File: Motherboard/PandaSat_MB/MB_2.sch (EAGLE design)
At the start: 70 parts, among them J1 503182-1852, J2 10118194-0001LF, J3 DCJ0303, Q10 IRLML5103, Q11 IRLML5103, Q13 IRLML2803, Q14 IRLML2803, Q15 IRLML2803, Q16 IRLML5103, Q17 2N5088, U1 MAX706R, U20 MR25H40MDF, U3 LSM9DS1, U4 PE014006, U5 MAX4372TEUK+T, U6 RFM23BP, U7 TPS54226PWPRPWP14_2P31X2P46-L, U8 ATSAMD51, X1 BU-SMA-V

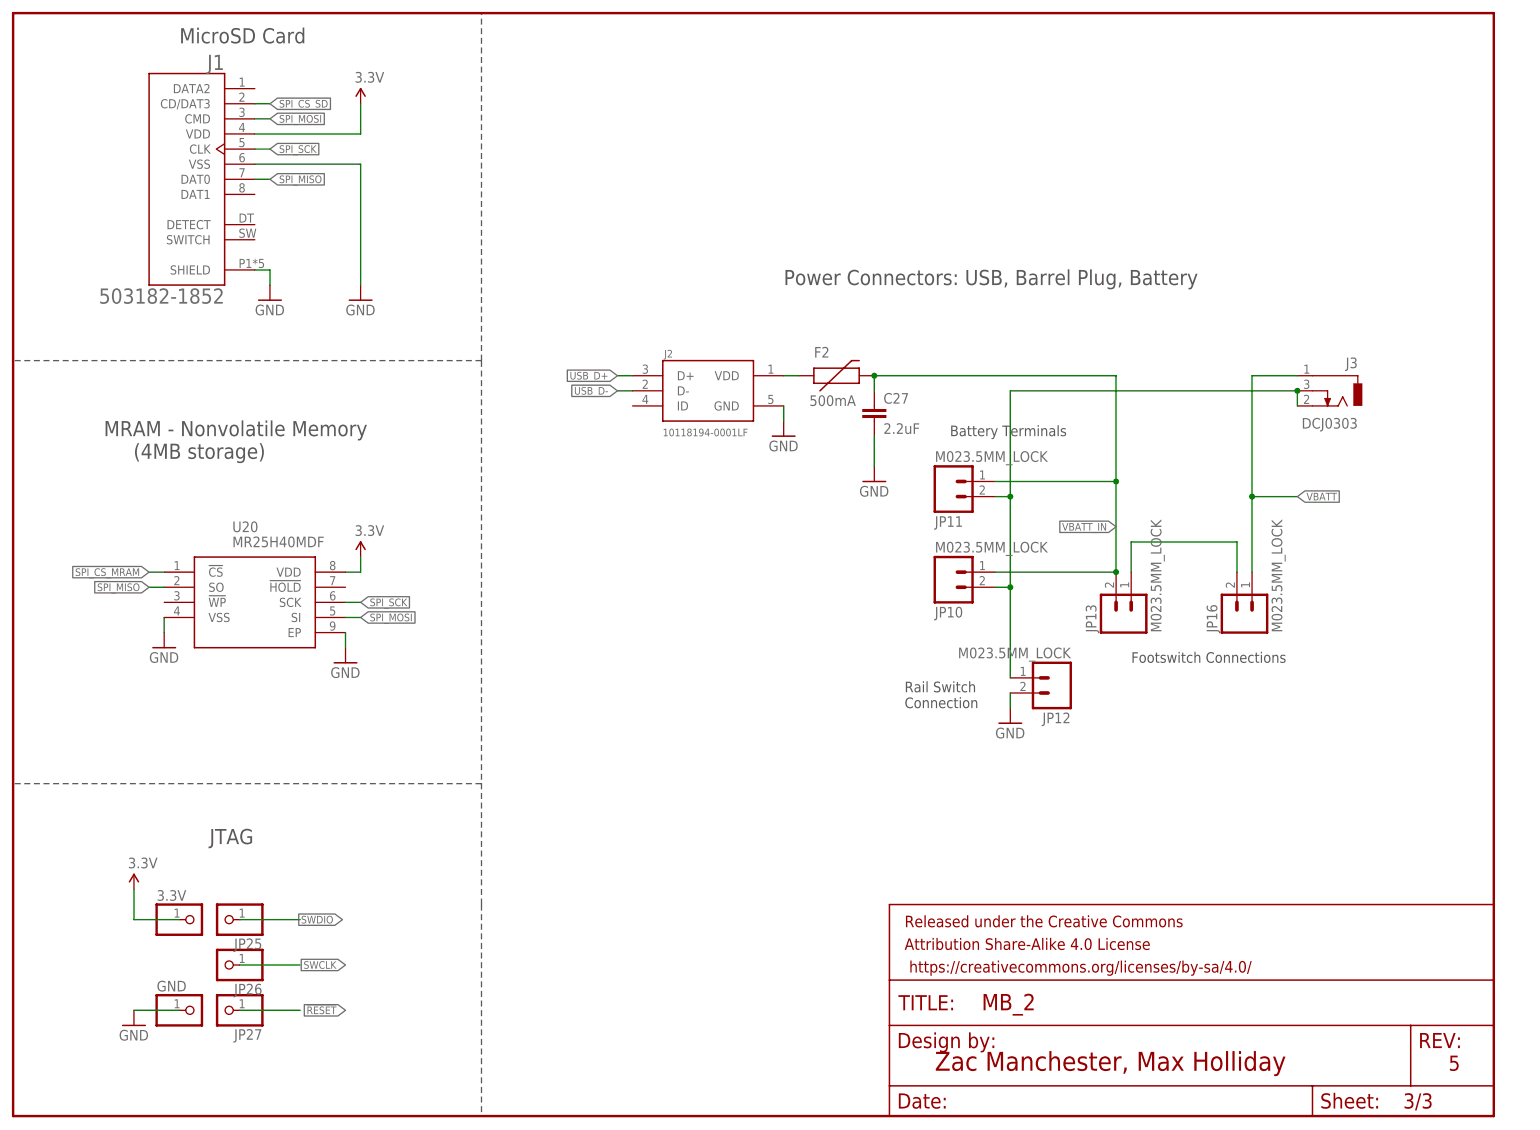
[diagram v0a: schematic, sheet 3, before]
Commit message: Added datasheets
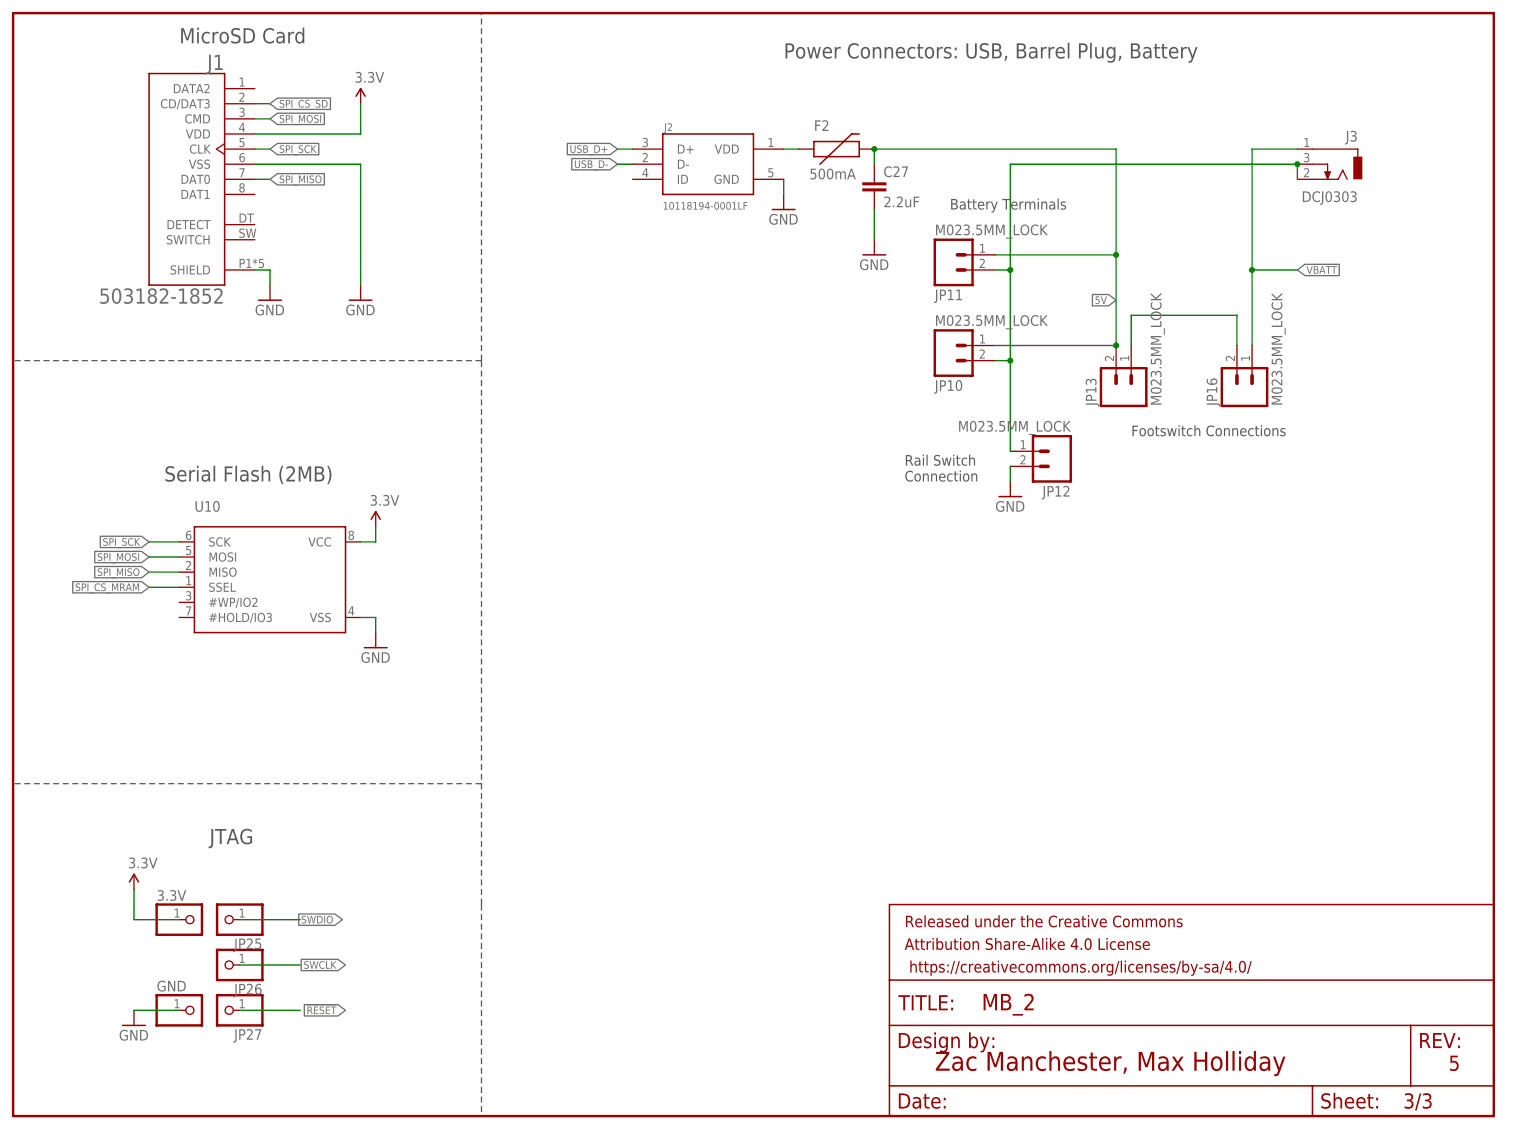
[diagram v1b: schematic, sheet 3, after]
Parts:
- removed U20: MR25H40MDF, maholli:MR25H40MDF
- added JP5: JUMPER-PAD-3-2OF3_NC_BY_TRACE_SMALL, SparkFun-Passives:JUMPER-PAD-3-2OF3_NC_BY_TRACE_SMALL
- added U10: (no value), microbuilder:SPIFLASH_SOIC8
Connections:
- removed net VBATT_IN: C27.1, F2.2, JP10.1, JP11.1, JP13.2
- new net 5V: C27.1, F2.2, JP10.1, JP11.1, JP13.2, U6.VCC
- new net N$1: JP5.2, U1.!WDO
- new net N$5: JP5.1, U1.!RESET
- net !RESET: now also JP5.3; no longer U1.!RESET, U1.!WDO
- net 3.3V: now also U10.VCC; no longer U20.VDD, U6.VCC
- net GND: now also U10.VSS; no longer U20.EP, U20.VSS
- net SPI_CS_MRAM: now also U10.SSEL; no longer U20.!CS
- net SPI_MISO: now also U10.MISO; no longer U20.SO
- net SPI_MOSI: now also U10.MOSI; no longer U20.SI
- net SPI_SCK: now also U10.SCK; no longer U20.SCK
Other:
- note added: "Serial Flash (2MB)"
- note removed: "MRAM - Nonvolatile Memory (4MB storage)"
- moved on the sheet: C27, F2, J2, J3, JP10, JP11, JP12, JP13, JP16

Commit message: Put charging circuit back in
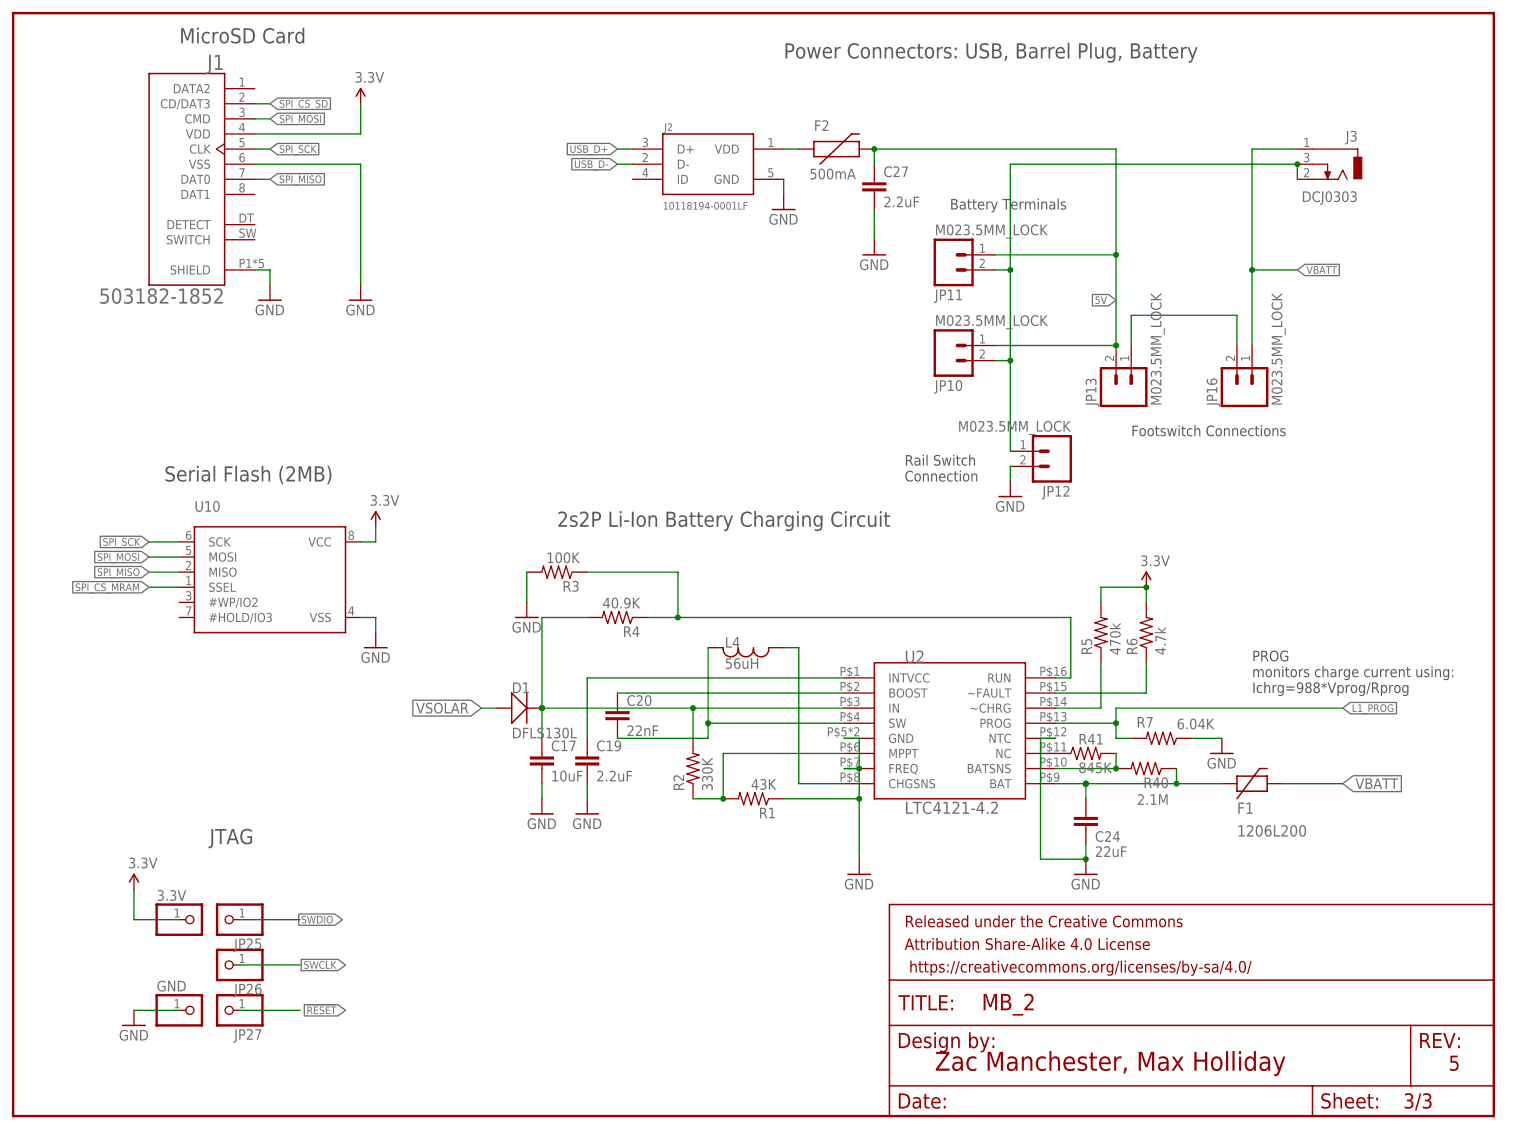
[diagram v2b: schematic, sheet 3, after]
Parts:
- added C17: 10uF, SparkFun-Capacitors:10UF-0603-6.3V-20%
- added C19: 2.2uF, SparkFun-Capacitors:2.2UF-0603-10V-20%
- added C20: 22nF, SparkFun-Capacitors:2.2NF/2200PF-0603-50V-10%
- added C24: 22uF, SparkFun-Capacitors:0.1UF-0603-25V-5%
- added D1: DFLS130L, BrownSpaceEngineering:DFLS130L
- added F1: 1206L200, BrownSpaceEngineering:PTCFUSE1206
- added L4: 56uH, BrownSpaceEngineering:IND1812
- added R1: 43K, resistor:R-US_R0603
- added R2: 330K, resistor:R-US_R0603
- added R3: 100K, resistor:R-US_R0603
- added R4: 40.9K, resistor:R-US_R0603
- added R40: 2.1M, resistor:R-US_R0603
- added R41: 845K, resistor:R-US_R0603
- added R5: 470k, resistor:R-US_R0603
- added R6: 4.7k, resistor:R-US_R0603
- added R7: 6.04K, resistor:R-US_R0603
- added U2: LTC4121-4.2, BrownSpaceEngineering:LTC4121-4.2
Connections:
- new net L1_CHG: R3.1, R4.1, U2.RUN
- new net L1_FAULTN: R6.1, U2.~FAULT
- new net L1_PROG: R7.2, U2.PROG
- new net LION1: C24.1, F1.P$1, R40.1, U2.BAT
- new net N$11: C19.1, U2.INTVCC
- new net N$13: R1.2, R2.1, U2.MPPT
- new net N$15: L4.P$2, U2.CHGSNS
- new net N$16: R5.1, U2.~CHRG
- new net N$17: R40.2, R41.2, U2.BATSNS
- new net N$54: R41.1, U2.NC
- new net N$7: C20.2, L4.P$1, U2.SW
- new net N$9: C20.1, U2.BOOST
- new net VSOLAR_IN: C17.1, D1.C, R2.2, R4.2, U2.IN
- net 3.3V: now also R5.2, R6.2
- net GND: now also C17.2, C19.2, C24.2, R1.1, R3.2, R7.1, U2.FREQ, U2.GND, U2.NTC
- net VBATT: now also F1.P$2
- net VSOLAR: now also D1.A
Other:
- note added: "2s2P Li-Ion Battery Charging Circuit"
- note added: "PROG monitors charge current using: Ichrg=988*Vprog/Rprog"
